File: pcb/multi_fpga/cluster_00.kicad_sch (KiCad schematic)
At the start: 7 parts, among them J1 Cluster0_SpokeBus, J2 Cluster0_Power

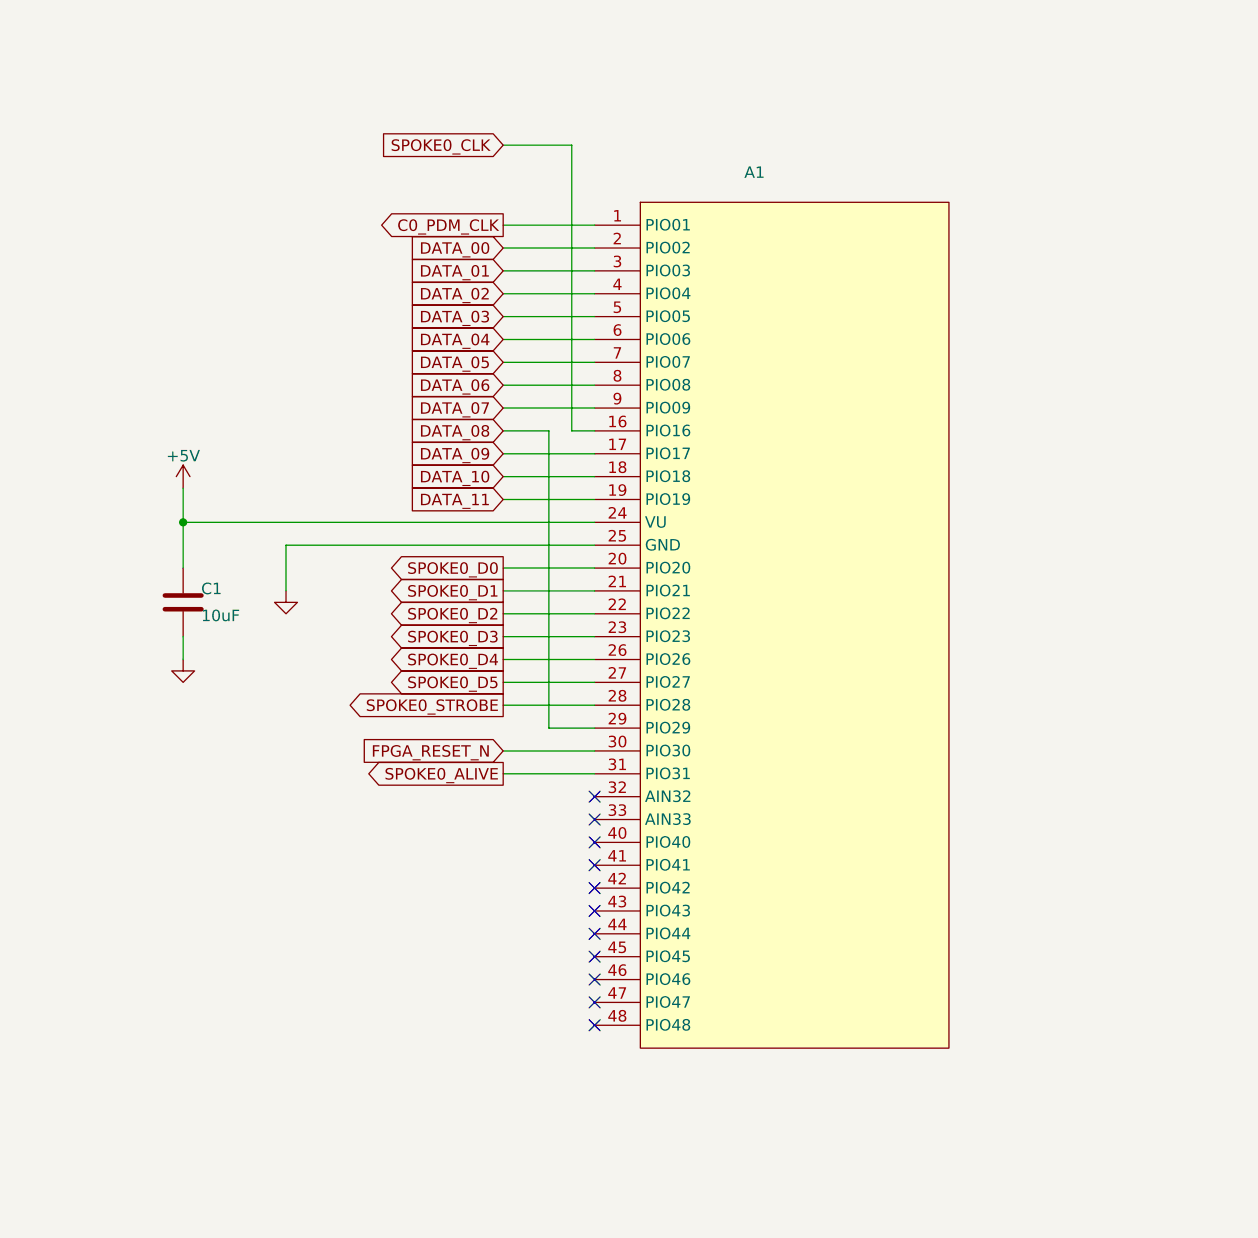
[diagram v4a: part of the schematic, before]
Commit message: Changed CMOD-S7 to CMOD-A7 to fit design.
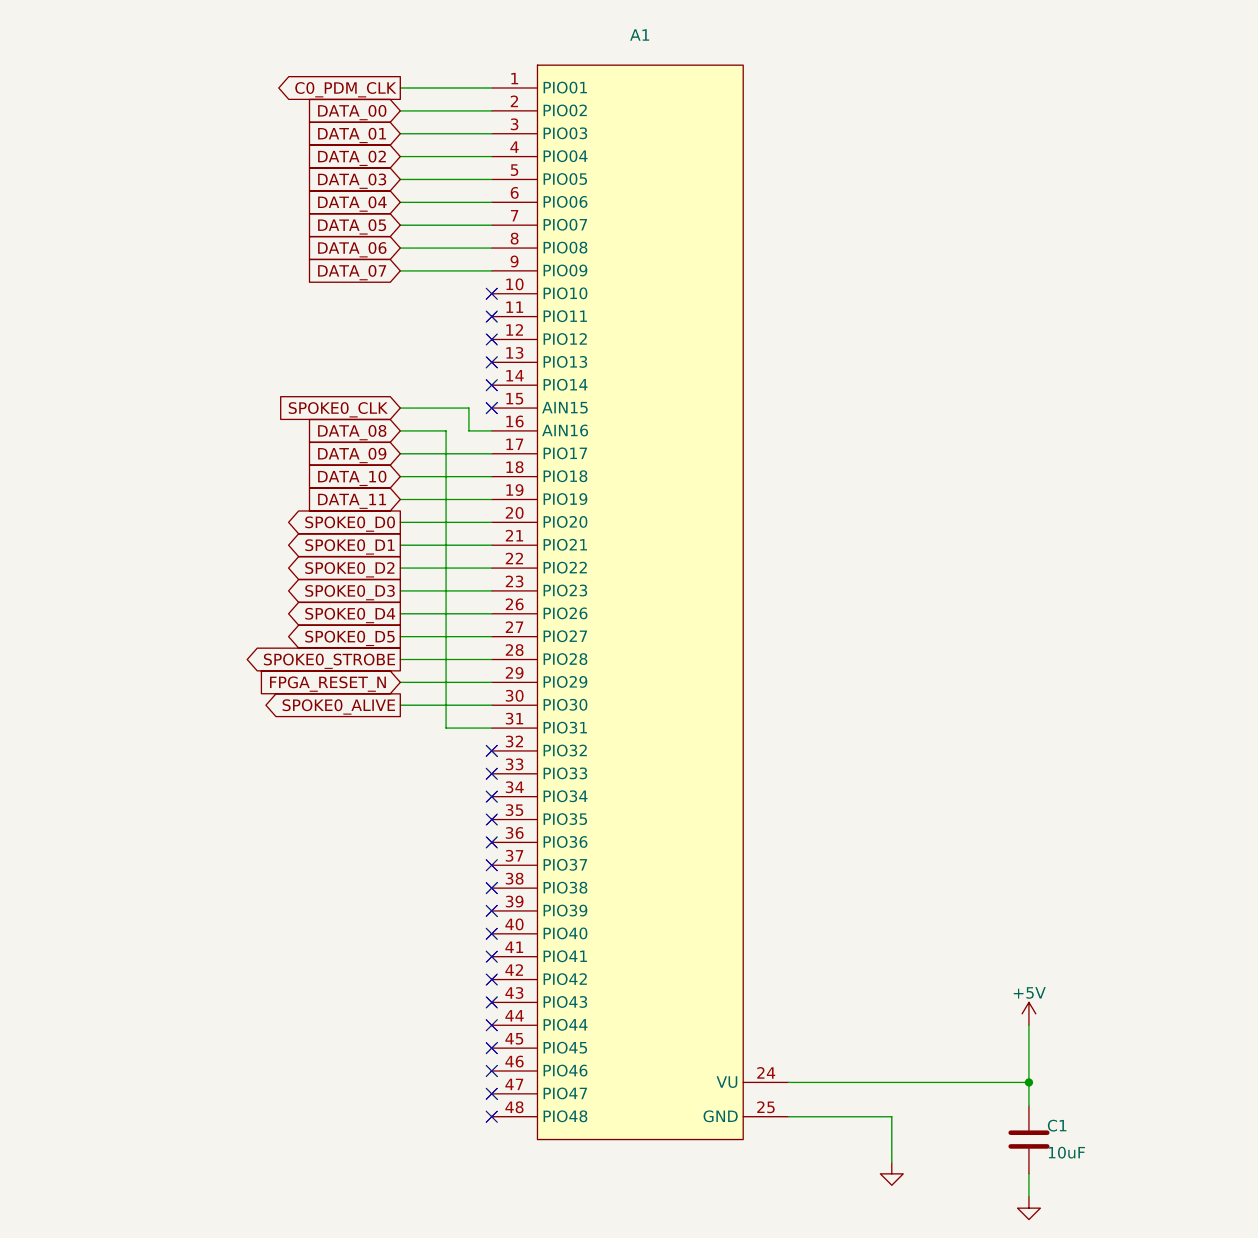
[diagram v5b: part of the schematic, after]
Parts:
- A1: symbol multi_fpga:CMOD_S7 -> multi_fpga:CMOD_A7_35T
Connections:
- net DATA_08: now also A1.31 (PIO31); no longer A1.29 (PIO29)
- net FPGA_RESET_N: now also A1.29 (PIO29); no longer A1.30 (PIO30)
- net SPOKE0_ALIVE: now also A1.30 (PIO30); no longer A1.31 (PIO31)
- no-connect marks 11 -> 23
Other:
- moved on the sheet: C1

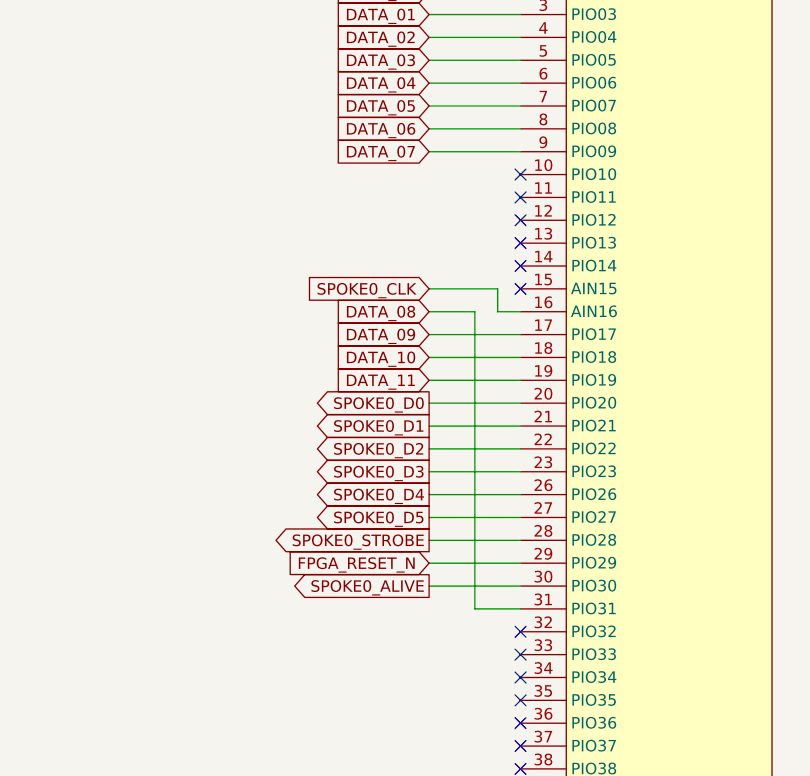
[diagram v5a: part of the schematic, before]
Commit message: Swapped to proper clock pin.
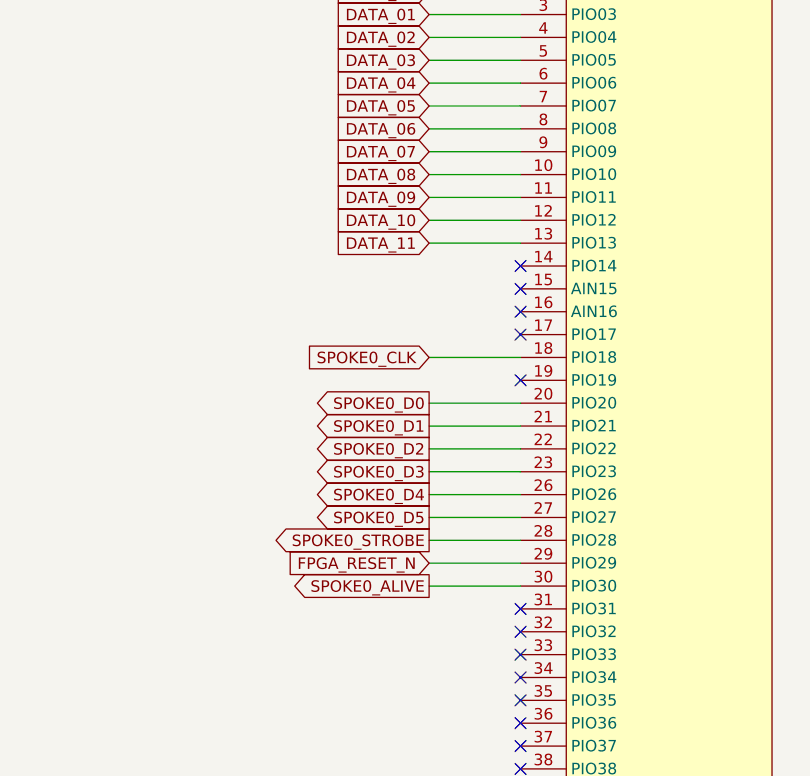
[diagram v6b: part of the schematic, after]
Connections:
- net DATA_08: now also A1.10 (PIO10); no longer A1.31 (PIO31)
- net DATA_09: now also A1.11 (PIO11); no longer A1.17 (PIO17)
- net DATA_10: now also A1.12 (PIO12); no longer A1.18 (PIO18)
- net DATA_11: now also A1.13 (PIO13); no longer A1.19 (PIO19)
- net SPOKE0_CLK: now also A1.18 (PIO18); no longer A1.16 (AIN16)
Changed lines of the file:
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@@
-	)
-	(no_connect
-		(at 193.04 124.46)
 	)
 	(no_connect
@@
 	)
 	(no_connect
+		(at 193.04 165.1)
+	)
+	(no_connect
 		(at 193.04 208.28)
 	)
 	(no_connect
-		(at 193.04 116.84)
+		(at 193.04 132.08)
 	)
 	(no_connect
@@
 	)
 	(no_connect
-		(at 193.04 119.38)
+		(at 193.04 134.62)
 	)
 	(no_connect
@@
 	)
 	(no_connect
-		(at 193.04 121.92)
+		(at 193.04 139.7)
 	)
 	(no_connect
@@
 	(wire
 		(pts
-			(xy 193.04 165.1) (xy 187.96 165.1)
-		)
-		(stroke
-			(width 0)
-			(type default)
-		)
-	)
-	(wire
-		(pts
 			(xy 182.88 152.4) (xy 193.04 152.4)
 		)
@@
 	(wire
 		(pts
-			(xy 193.04 139.7) (xy 182.88 139.7)
-		)
-		(stroke
-			(width 0)
-			(type default)
-		)
-	)
-	(wire
-		(pts
-			(xy 193.04 134.62) (xy 182.88 134.62)
-		)
-		(stroke
-			(width 0)
-			(type default)
-		)
-	)
-	(wire
-		(pts
 			(xy 182.88 149.86) (xy 193.04 149.86)
 		)
@@
 	(wire
 		(pts
+			(xy 182.88 116.84) (xy 193.04 116.84)
+		)
+		(stroke
+			(width 0)
+			(type default)
+		)
+	)
+	(wire
+		(pts
 			(xy 226.06 208.28) (xy 237.49 208.28)
 		)
@@
 	(wire
 		(pts
+			(xy 182.88 137.16) (xy 193.04 137.16)
+		)
+		(stroke
+			(width 0)
+			(type default)
+		)
+	)
+	(wire
+		(pts
 			(xy 237.49 213.36) (xy 237.49 208.28)
 		)
@@
 	(wire
 		(pts
+			(xy 182.88 119.38) (xy 193.04 119.38)
+		)
+		(stroke
+			(width 0)
+			(type default)
+		)
+	)
+	(wire
+		(pts
 			(xy 331.47 111.76) (xy 342.9 111.76)
 		)
@@
 	(wire
 		(pts
-			(xy 182.88 132.08) (xy 187.96 132.08)
-		)
-		(stroke
-			(width 0)
-			(type default)
-		)
-	)
-	(wire
-		(pts
 			(xy 327.66 181.61) (xy 327.66 189.23)
 		)
@@
 	(wire
 		(pts
-			(xy 190.5 132.08) (xy 193.04 132.08)
-		)
-		(stroke
-			(width 0)
-			(type default)
-		)
-	)
-	(wire
-		(pts
-			(xy 190.5 129.54) (xy 190.5 132.08)
-		)
-		(stroke
-			(width 0)
-			(type default)
-		)
-	)
-	(wire
-		(pts
 			(xy 358.14 185.42) (xy 358.14 189.23)
 		)
@@
 	(wire
 		(pts
-			(xy 182.88 129.54) (xy 190.5 129.54)
+			(xy 182.88 124.46) (xy 193.04 124.46)
 		)
 		(stroke
@@
 	(wire
 		(pts
-			(xy 187.96 132.08) (xy 187.96 165.1)
-		)
-		(stroke
-			(width 0)
-			(type default)
-		)
-	)
-	(wire
-		(pts
 			(xy 358.14 195.58) (xy 358.14 191.77)
 		)
@@
 	(wire
 		(pts
-			(xy 193.04 137.16) (xy 182.88 137.16)
-		)
-		(stroke
-			(width 0)
-			(type default)
-		)
-	)
-	(wire
-		(pts
 			(xy 309.88 119.38) (xy 318.77 119.38)
+		)
+		(stroke
+			(width 0)
+			(type default)
+		)
+	)
+	(wire
+		(pts
+			(xy 182.88 121.92) (xy 193.04 121.92)
 		)
 		(stroke
@@
 	(global_label "DATA_11"
 		(shape input)
-		(at 182.88 139.7 180)
-		(effects
-			(font
-				(size 1.27 1.27)
-			)
-			(justify right)
-		)
-		(property "Intersheetrefs" "${INTERSHEET_REFS}"
-			(at 182.88 139.7 180)
+		(at 182.88 124.46 180)
+		(effects
+			(font
+				(size 1.27 1.27)
+			)
+			(justify right)
+		)
+		(property "Intersheetrefs" "${INTERSHEET_REFS}"
+			(at 182.88 124.46 180)
 			(hide yes)
 			(show_name no)
@@
 	(global_label "SPOKE0_CLK"
 		(shape input)
-		(at 182.88 129.54 180)
-		(effects
-			(font
-				(size 1.27 1.27)
-			)
-			(justify right)
-		)
-		(property "Intersheetrefs" "${INTERSHEET_REFS}"
-			(at 182.88 129.54 180)
+		(at 182.88 137.16 180)
+		(effects
+			(font
+				(size 1.27 1.27)
+			)
+			(justify right)
+		)
+		(property "Intersheetrefs" "${INTERSHEET_REFS}"
+			(at 182.88 137.16 180)
 			(hide yes)
 			(show_name no)
@@
 	(global_label "DATA_08"
 		(shape input)
-		(at 182.88 132.08 180)
-		(effects
-			(font
-				(size 1.27 1.27)
-			)
-			(justify right)
-		)
-		(property "Intersheetrefs" "${INTERSHEET_REFS}"
-			(at 182.88 132.08 180)
+		(at 182.88 116.84 180)
+		(effects
+			(font
+				(size 1.27 1.27)
+			)
+			(justify right)
+		)
+		(property "Intersheetrefs" "${INTERSHEET_REFS}"
+			(at 182.88 116.84 180)
 			(hide yes)
 			(show_name no)
@@
 	(global_label "DATA_10"
 		(shape input)
-		(at 182.88 137.16 180)
-		(effects
-			(font
-				(size 1.27 1.27)
-			)
-			(justify right)
-		)
-		(property "Intersheetrefs" "${INTERSHEET_REFS}"
-			(at 182.88 137.16 180)
+		(at 182.88 121.92 180)
+		(effects
+			(font
+				(size 1.27 1.27)
+			)
+			(justify right)
+		)
+		(property "Intersheetrefs" "${INTERSHEET_REFS}"
+			(at 182.88 121.92 180)
 			(hide yes)
 			(show_name no)
@@
 	(global_label "DATA_09"
 		(shape input)
-		(at 182.88 134.62 180)
-		(effects
-			(font
-				(size 1.27 1.27)
-			)
-			(justify right)
-		)
-		(property "Intersheetrefs" "${INTERSHEET_REFS}"
-			(at 182.88 134.62 180)
-			(hide yes)
-			(show_name no)
+		(at 182.88 119.38 180)
+		(effects
+			(font
+				(size 1.27 1.27)
+			)
+			(justify right)
+		)
+		(property "Intersheetrefs" "${INTERSHEET_REFS}"
+			(at 182.88 119.38 180)
+			(hide yes)
+			(show_name no)

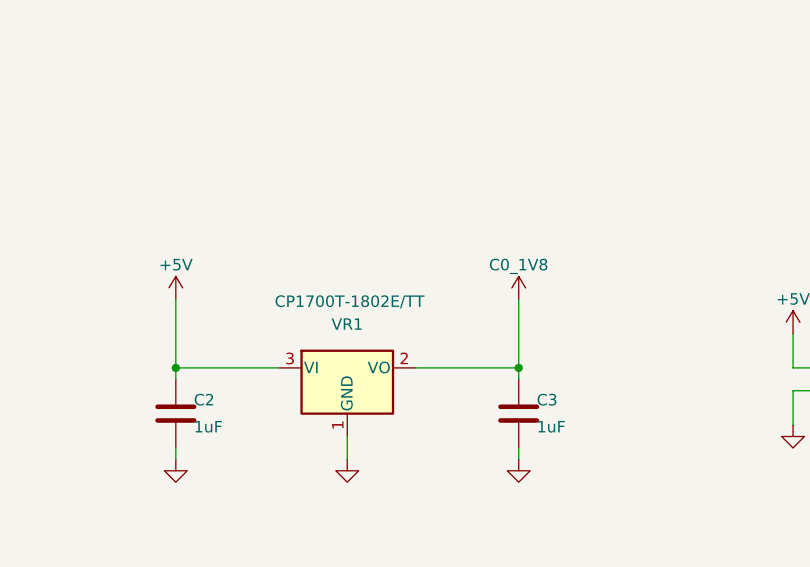
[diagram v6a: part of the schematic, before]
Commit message: Changed mic signals and LDOs to 3V3.
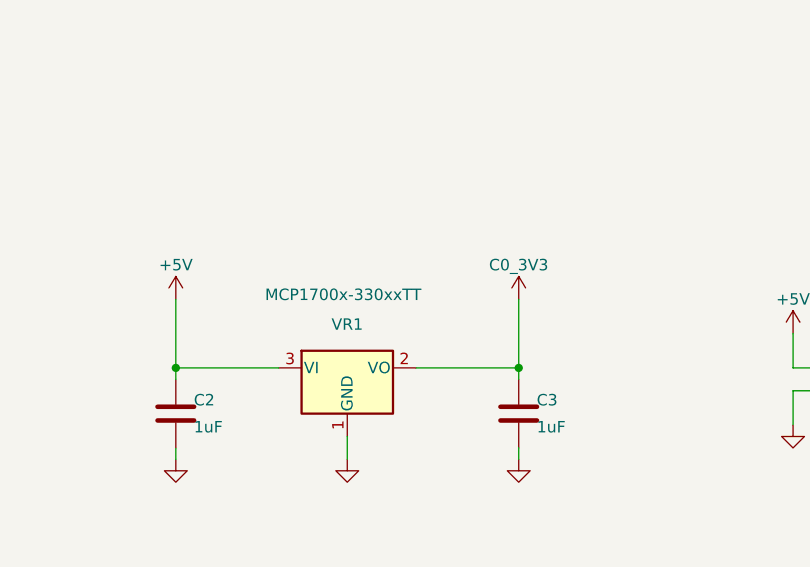
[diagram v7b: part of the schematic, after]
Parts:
- VR1: value CP1700T-1802E/TT -> MCP1700x-330xxTT; symbol Regulator_Linear:MCP1700x-180xxTT -> Regulator_Linear:MCP1700x-330xxTT
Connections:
- net C0_1V8 renamed C0_3V3
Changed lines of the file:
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@@
 	)
 	(symbol
-		(lib_id "multi_fpga:C0_1V8")
+		(lib_id "multi_fpga:C0_3V3")
 		(at 327.66 181.61 0)
 		(unit 1)
@@
 			)
 		)
-		(property "Value" "C0_1V8"
+		(property "Value" "C0_3V3"
 			(at 327.66 177.8 0)
 			(show_name no)
@@
 	)
 	(symbol
-		(lib_id "Regulator_Linear:MCP1700x-180xxTT")
+		(lib_id "Regulator_Linear:MCP1700x-330xxTT")
 		(at 308.61 189.23 0)
 		(unit 1)
@@
 			)
 		)
-		(property "Value" "CP1700T-1802E/TT"
-			(at 308.864 181.864 0)
+		(property "Value" "MCP1700x-330xxTT"
+			(at 299.466 181.102 0)
 			(show_name no)
 			(do_not_autoplace no)
@@
 					(size 1.27 1.27)
 				)
+				(justify left)
 			)
 		)
 		(property "Footprint" "Package_TO_SOT_SMD:SOT-23"
-			(at 308.61 189.23 0)
+			(at 308.61 183.515 0)
 			(hide yes)
 			(show_name no)
@@
 			)
 		)
-		(property "Description" "250mA Low Quiscent Current LDO, 1.8V output, SOT-23"
+		(property "Description" "250mA Low Quiscent Current LDO, 3.3V output, SOT-23"
 			(at 308.61 189.23 0)
 			(hide yes)

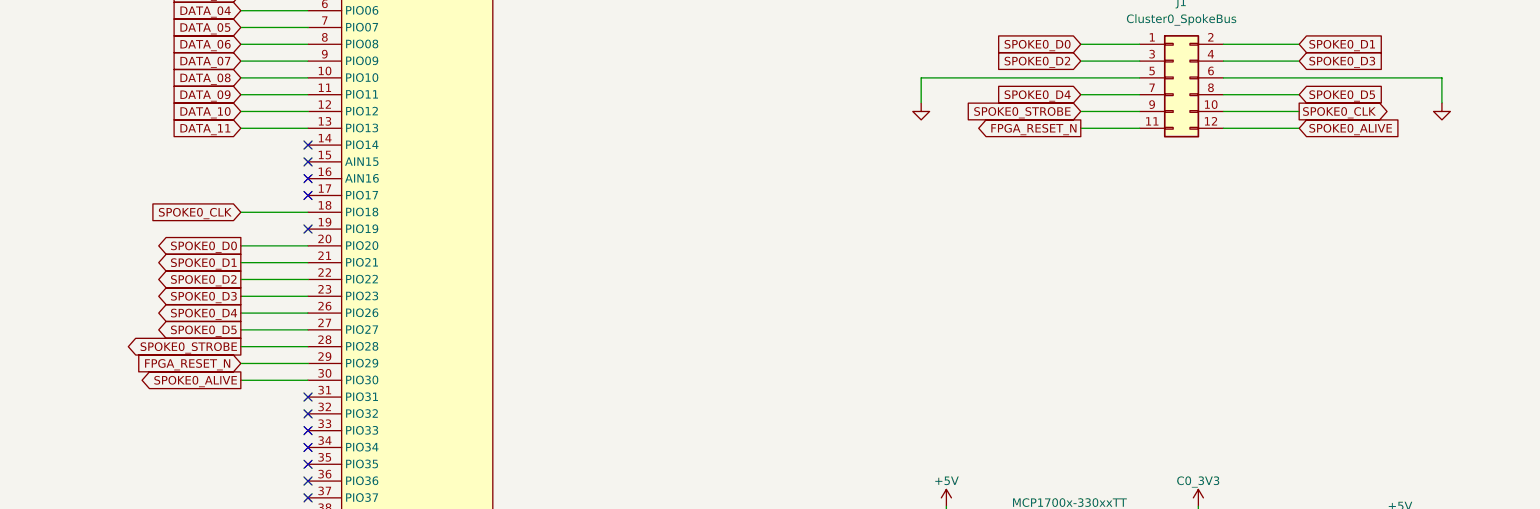
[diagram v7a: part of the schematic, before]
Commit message: Changed from per-spoke to shared spoke alive signals.
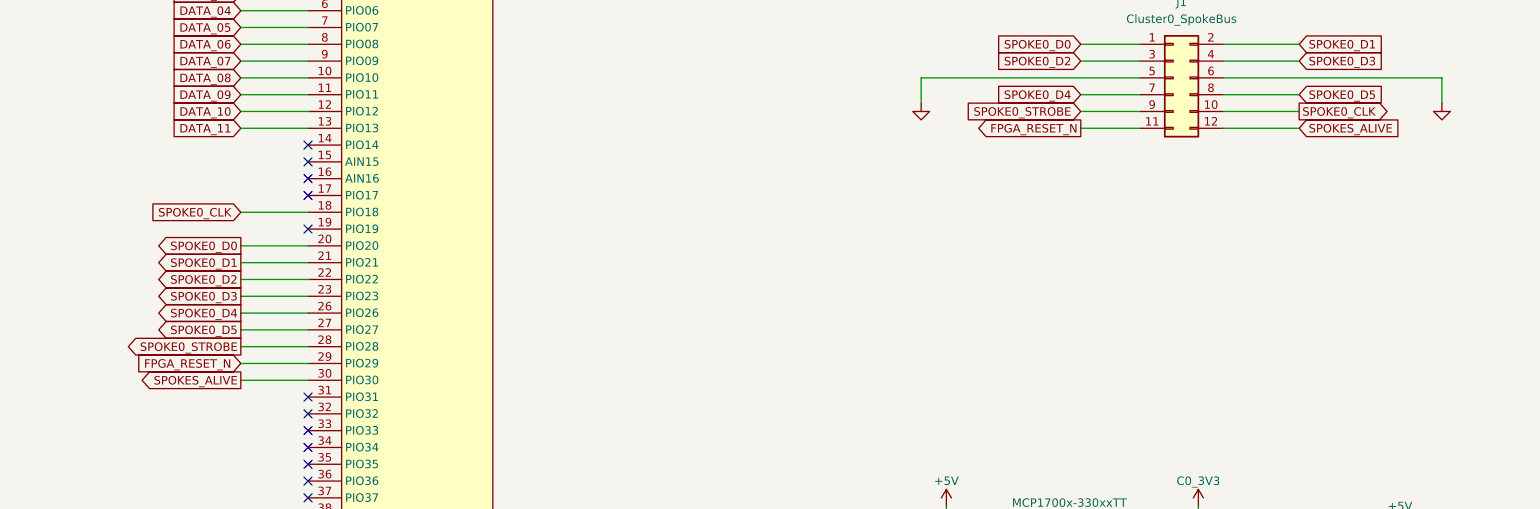
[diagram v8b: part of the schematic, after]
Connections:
- net SPOKE0_ALIVE renamed SPOKES_ALIVE
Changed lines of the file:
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@@
 		)
 	)
-	(global_label "SPOKE0_ALIVE"
+	(global_label "SPOKES_ALIVE"
 		(shape input)
 		(at 342.9 124.46 0)
@@
 		)
 	)
-	(global_label "SPOKE0_ALIVE"
+	(global_label "SPOKES_ALIVE"
 		(shape output)
 		(at 182.88 162.56 180)
